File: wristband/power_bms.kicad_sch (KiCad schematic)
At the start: 18 parts, among them J1 USB4125-GF-A, Q1 AO3401A, Q2 FS8205A, U1 DW01A, U2 MCP73831T-2ACI/OT

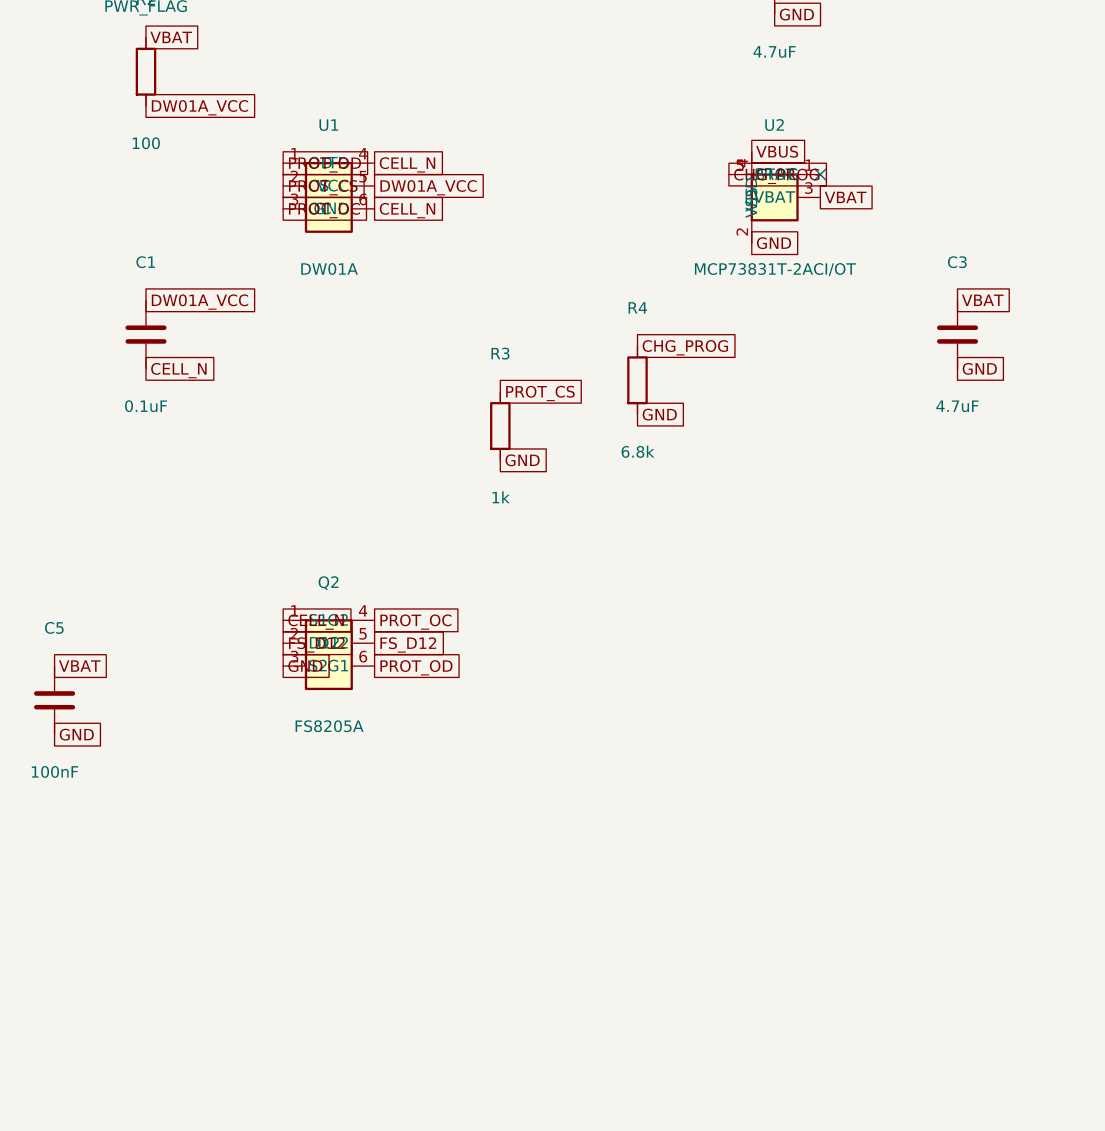
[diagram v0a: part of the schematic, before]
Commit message: Migrate wristband to NINA-B400, wire all sheets, close six design gaps
Replaces the wristband's u-blox NINA-B111 (nRF52832) with a NINA-B400-00B
(Nordic nRF52833, Bluetooth 5.1), then follows through on everything that
change and a full schematic review surfaced.

NINA-B400 migration
- New 55-pin + EGP + EAGP symbol, transcribed from the real NINA-B40 data
  sheet UBX-19049405 R09 Table 6 and cross-checked against Figure 3 for rank
  ordering. Pin numbering validated programmatically (1-55, each exactly once).
- NINA-B4 is pin/mechanically compatible with NINA-B3, NOT NINA-B1, so the
  42-pad NINA111-42 land pattern does not carry over. No official footprint
  exists anywhere -- u-blox's own Eagle library ships only NINA111-42/112-42,
  and neither KiCad's bundled nor upstream RF_Module library has a B3/B4 part.
  NINA-B400-55_PLACEHOLDER is therefore flagged: outline, pad count and rank
  arrangement are confirmed; individual pad X/Y are derived estimates.
  MUST be replaced before fabrication.
- B400 chosen over B401/B406 for its on-module U.FL connector, which let the
  PCB-side U.FL (J2) and the untuned L/C match network (L1/C13) be deleted --
  retiring the project's only open RF-tuning risk.
- No power-design impact: abs-max VCC is 3.9 V on both modules, so the MCP1700
  LDO rationale stands. Budget 12 mA -> 15.5 mA typ; ~70.5 mA with DWM3000
  against 250 mA, ~3.5x headroom (corrects a stale "3.7x" in the docs).
- SWD pin numbers are unchanged (SWDCLK=11, SWDIO=15, RESET_N=19, SWO=8).

Antenna re-verified, part number corrected
- The specified antenna is still pre-approved for NINA-B4 (certification app
  note UBX-20037320 R05 s3.2) but ProAnt was acquired by Abracon and u-blox
  now lists it as PRO-IS-237. Same specs throughout. Order under the Abracon PN.

Six gaps closed
- Y1 + C14/C15: 32.768 kHz LFXO (Epson FC-135, Q13FC13500004). Required for
  lowest sleep current per SIM UBX-19052230 R13 s1.9; XL1/XL2 were floating,
  which Table 6 does not permit eve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
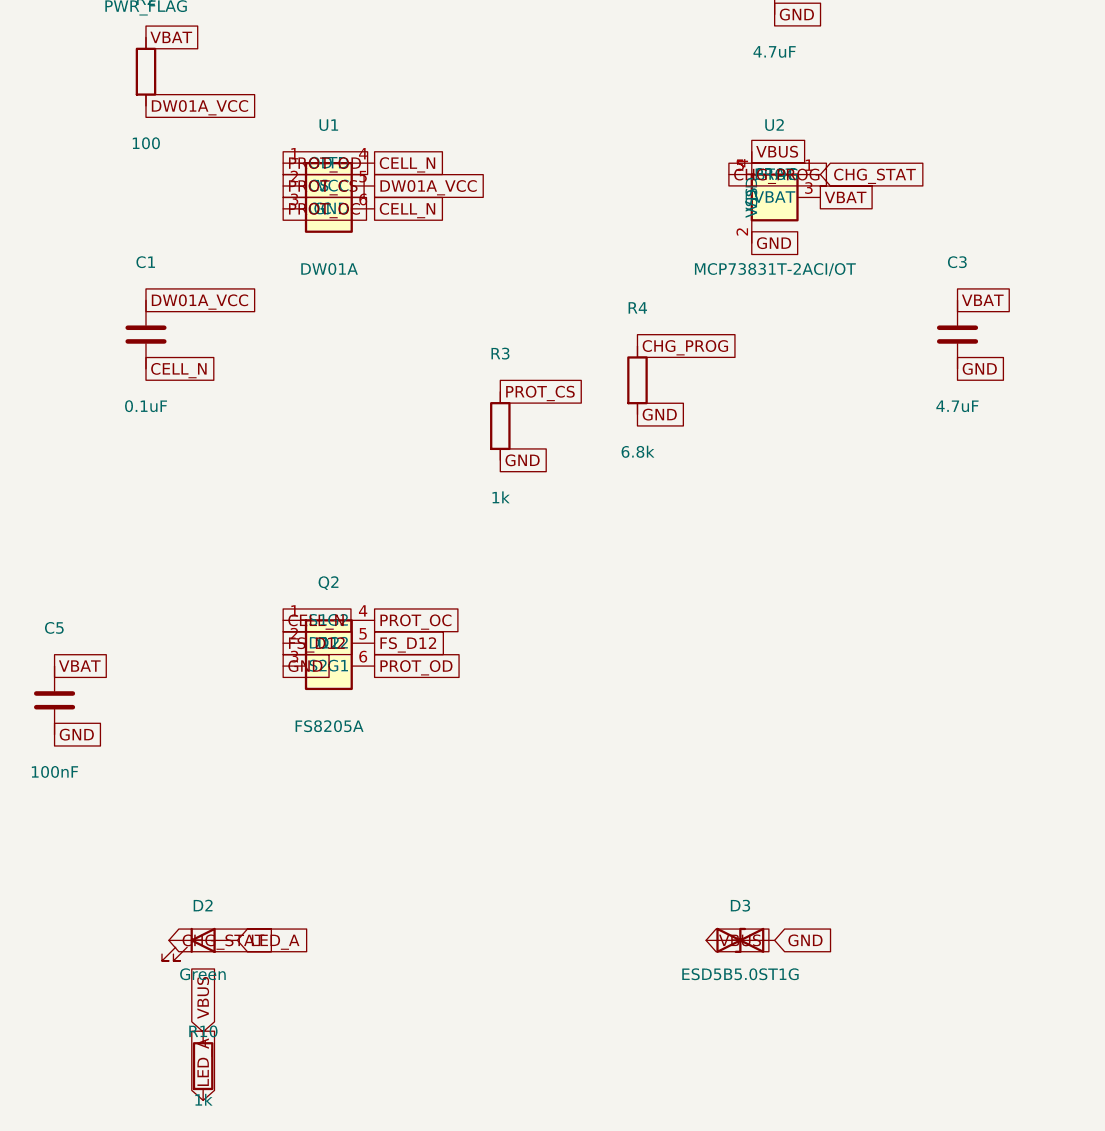
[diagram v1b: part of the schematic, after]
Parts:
- added D2: Green, LED_SMD:LED_0603_1608Metric, symbol Device:LED
- added D3: ESD5B5.0ST1G, Diode_SMD:D_SOD-523, symbol Device:D_TVS
- added R10: 1k, Resistor_SMD:R_0603_1608Metric, symbol Device:R
- C1, C5: MPN (none) -> CL10B104KB8NNNC; Manufacturer (none) -> Samsung Electro-Mechanics
- C2, C3: MPN (none) -> CL10A475KO8NNNC; Manufacturer (none) -> Samsung Electro-Mechanics
- C4: MPN (none) -> CL10A106KP8NNNC; Manufacturer (none) -> Samsung Electro-Mechanics
- D1: MPN (none) -> ESD5B5.0ST1G; Manufacturer (none) -> onsemi
- J1: MPN (none) -> USB4125-GF-A; Manufacturer (none) -> GCT
- Q1: MPN (none) -> AO3401A; Manufacturer (none) -> Alpha & Omega Semiconductor
- Q2: MPN (none) -> FS8205; Manufacturer (none) -> Fortune Semiconductor
- R1: MPN (none) -> RC0603FR-07100KL; Manufacturer (none) -> Yageo
- R2: MPN (none) -> RC0603FR-13100RL; Manufacturer (none) -> Yageo
- R3: MPN (none) -> RC0603FR-071KL; Manufacturer (none) -> Yageo
- R4: MPN (none) -> RC0603FR-076K8L; Manufacturer (none) -> Yageo
- R5, R6: MPN (none) -> RC0603FR-075K1L; Manufacturer (none) -> Yageo
- U1: MPN (none) -> DW01A; Manufacturer (none) -> Fortune Semiconductor
- U2: MPN (none) -> MCP73831T-2ACI/OT; Manufacturer (none) -> Microchip
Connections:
- net GND: now also D3.2 (A2)
- net VBUS: now also D3.1 (A1), R10.1
- net CHG_STAT: now reaches U2.1 (STAT)
- net CHG_STAT: now also D2.1 (K)
- new net LED_A: D2.2 (A), R10.2
- no-connect marks 1 -> 0

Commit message: Make schematics readable: wire stubs, A3 reflow, DWM3000 symbol redraw
Connectivity is unchanged -- verified by diffing the exported netlist against
the previous commit: 34 nets, identical pin membership on every one. This is
presentation only.

The problem was pre-existing, not new. Labels were placed exactly on the pin
endpoint, so label text printed on top of the symbol's own pin name (+3V3
stamped over VCC, UWB_CS over GPIO_1). power_bms had it on U1/U2/Q2 as well;
it only became obvious when the convention was scaled onto a 55-pin part.
Every label now sits at the end of a short wire stub pointing away from the
body, which is the standard KiCad idiom.

DWM3000 symbol redrawn (shared/symbols/)
- The old symbol was a 20mm square carrying pin names like GPIO0/RXOKLED drawn
  vertically along the bottom edge, where they collided with each other inside
  the symbol. No amount of label placement fixes that.
- Now 56 x 41mm, functionally grouped: power/ground/control left, SPI/GPIO
  right, no bottom-edge pins. All 24 pins and every property preserved.
- Checked the blast radius before touching it: bay-station is entirely unwired
  (0 wires, 0 labels on every sheet), so nothing was orphaned. Its cached copy
  is refreshed here and its netlist still exports cleanly at 75 components.

Layout
- radio_mcu and power_bms moved to A3 and reflowed into functional blocks;
  42 symbols repositioned.
- 38 annotations added, carrying the datasheet citations and reasoning that
  previously lived only in the markdown -- LFXO load-cap derivation, the
  ~2.1uA battery-divider tradeoff, why DW01A's GND sits on CELL_N, the LDO
  headroom budget, and the unchanged-from-NINA-B111 SWD pin numbers.

Verification
- Wrote a text-collision checker rather than eyeballing it. It caught two
  classes of bug: duplicated annotations (strip() cleared labels and wires but
  not text, so a second pass layered notes over old ones) and doubled labels on
  stacked same-net pins (USB-C J1 A9/B9, A12/B12;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
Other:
- note added: "Battery input + reverse-polarity protection"
- note added: "Bulk / bypass on the protected VBAT rail"
- note added: "Cell protection -- DW01A (U1) + FS8205 dual FET (Q2)"
- note added: "Charge status LED -- ~1.3mA via R10 while STAT sinks"
- note added: "Q1 AO3401A as an ideal diode -- no series voltage drop"
- note added: "R5/R6 are the 5.1k CC pull-downs; J1 is power-only (no D+/D-)"
- note added: "U1's GND sits on CELL_N (raw cell -), before the pass FETs,"
- note added: "USB-C charging -- MCP73831, ~147mA set by R4"
- note added: "VBUS ESD -- place close to J1"
- note added: "exactly where Fortune's own application circuit draws it."
- moved on the sheet: BT1, C1, C2, C3, C4, C5, D1, D2, D3, J1, Q1, Q2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
